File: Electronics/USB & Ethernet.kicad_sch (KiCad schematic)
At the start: 13 parts, among them IC4 USB2512B-AEZG, J22 USB_A_Stacked, Y3 30MHz

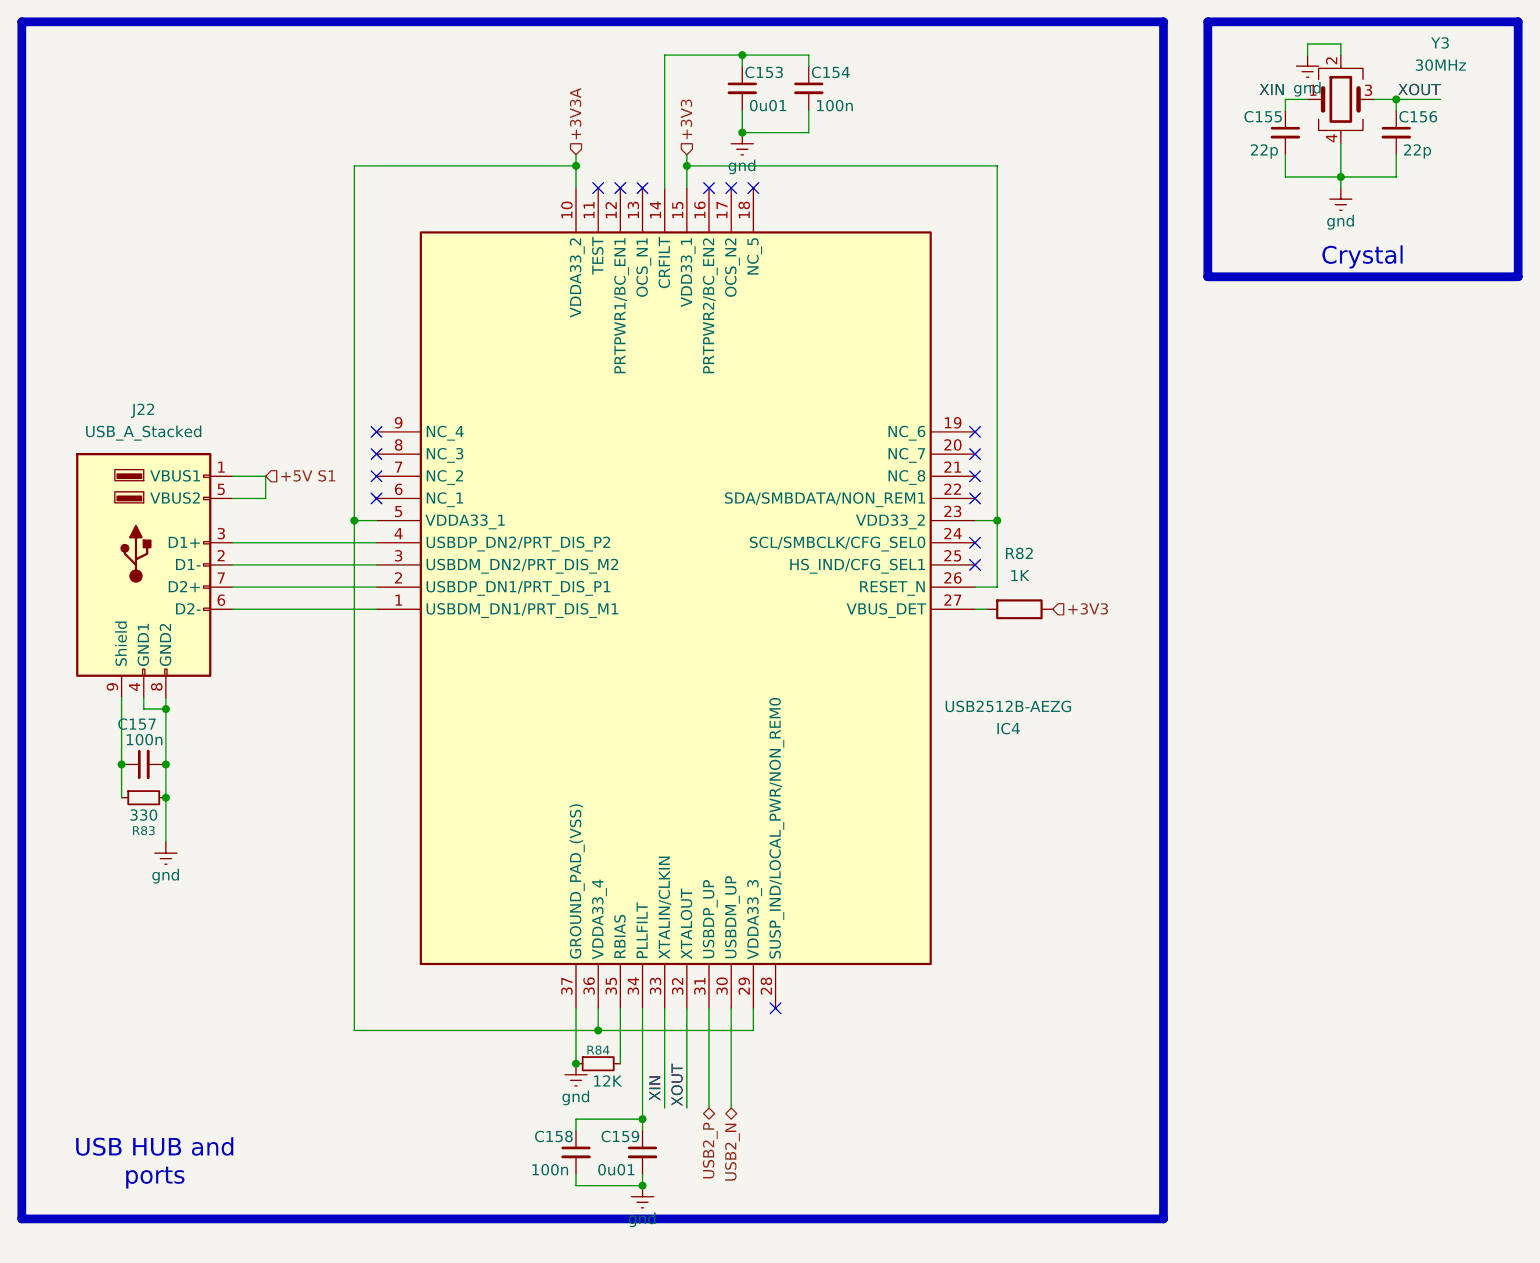
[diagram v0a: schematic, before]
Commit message: More pcb arangment, verticle ports
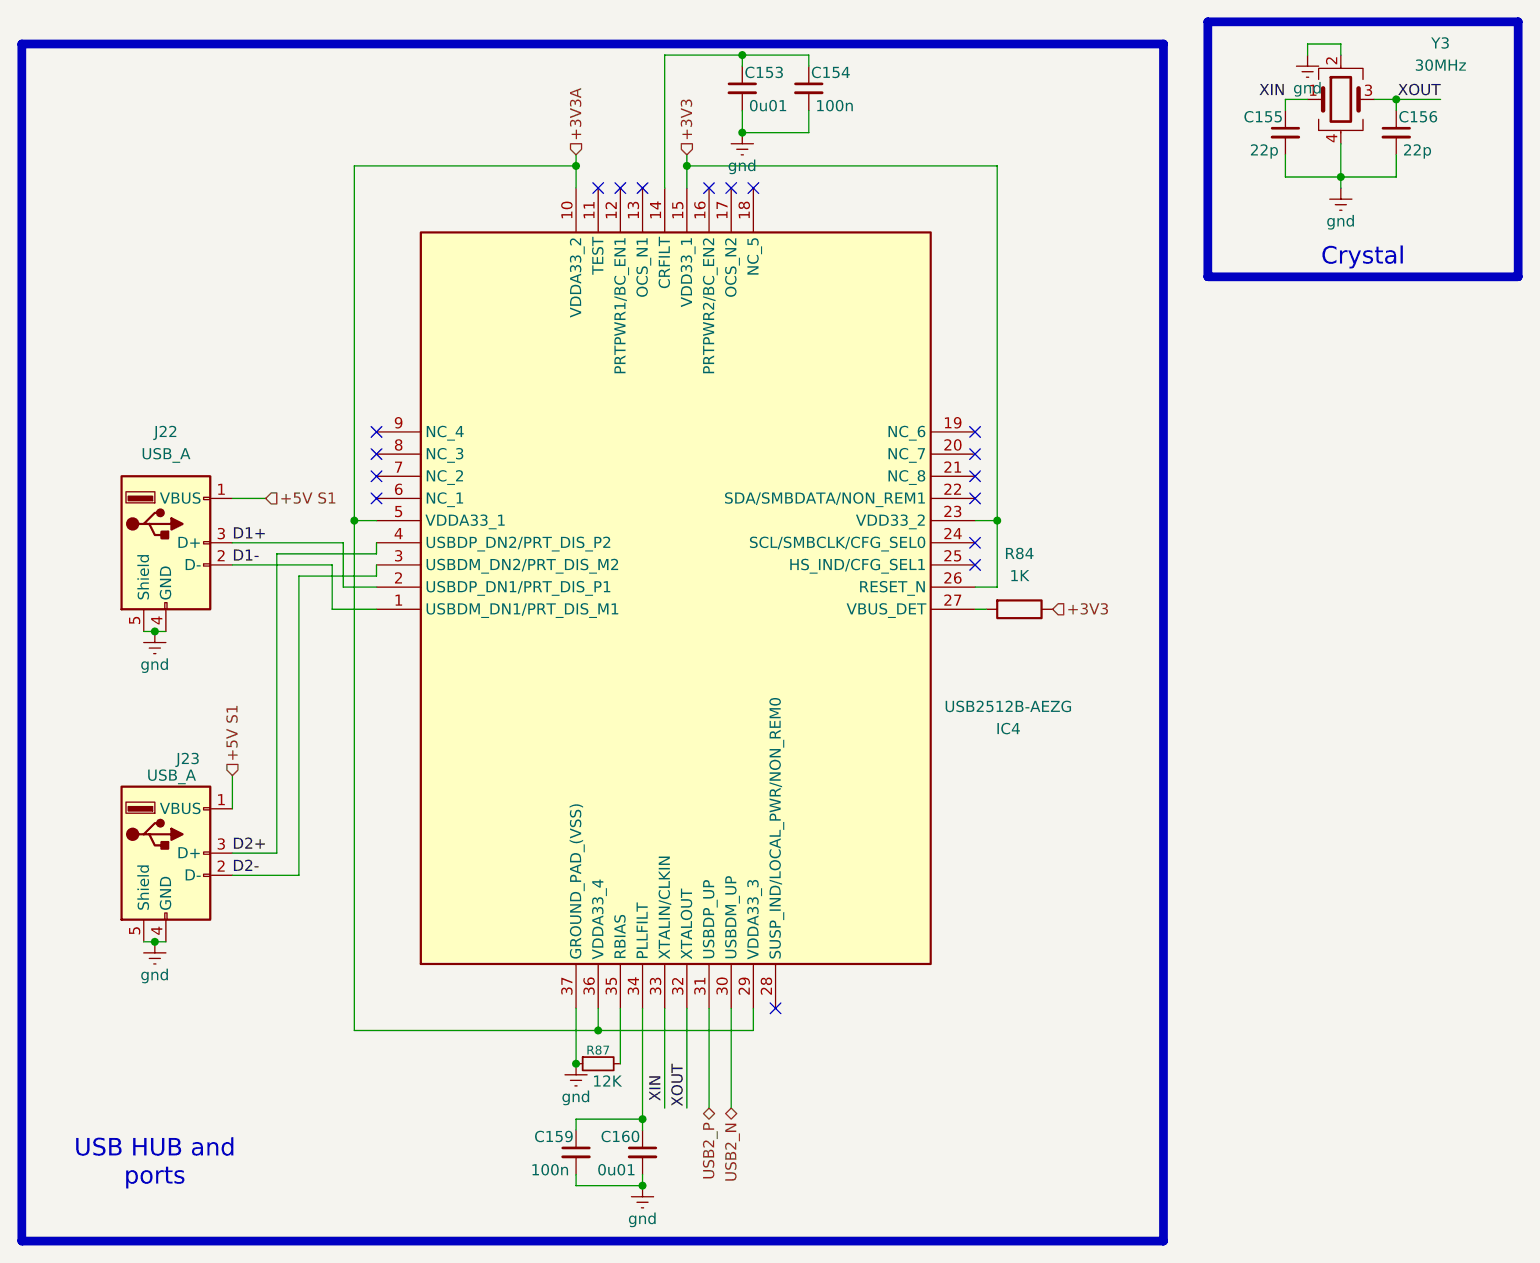
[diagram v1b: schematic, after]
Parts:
- removed C157: 100n, Capacitor_SMD:C_0603_1608Metric, symbol Device:C_Small
- removed J22: USB_A_Stacked, Connector_USB:USB_A_Wuerth_61400826021_Horizontal_Stacked, symbol Connector:USB_A_Stacked
- removed R83: 330, Resistor_SMD:R_0603_1608Metric, symbol Device:R_Small
- added J22, J23: USB_A, 482040001:CONN_48204-0001_MOL, symbol Connector:USB_A
- renumbered C158 to C159, C159 to C160, R82 to R84, R84 to R87
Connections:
- net +5V S1: now also J22.1 (VBUS), J23.1 (VBUS)
- net gnd: now also J22.4 (GND), J22.5 (Shield), J23.4 (GND), J23.5 (Shield)
- net D1-: now reaches IC4.1 (USBDM_DN1/PRT_DIS_M1)
- net D1-: now also J22.2 (D-)
- net D1+: now reaches IC4.2 (USBDP_DN1/PRT_DIS_P1)
- net D1+: now also J22.3 (D+)
- net D2-: now reaches IC4.3 (USBDM_DN2/PRT_DIS_M2)
- net D2-: now also J23.2 (D-)
- net D2+: now reaches IC4.4 (USBDP_DN2/PRT_DIS_P2)
- net D2+: now also J23.3 (D+)
